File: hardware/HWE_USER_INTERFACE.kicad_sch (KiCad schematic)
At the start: 19 parts, among them J10 OLED_DISPLAY_i2c, J11 ENC_VOLUME_LED-RING, J13 OLED_DISPLAY_SPI, J4 BTN_PLAY, J5 BTN_REC, J6 BTN_STOP, J7 BTN_QUANTISE, J8 BTN_OVERDUB, J9 BTN_METRONOME

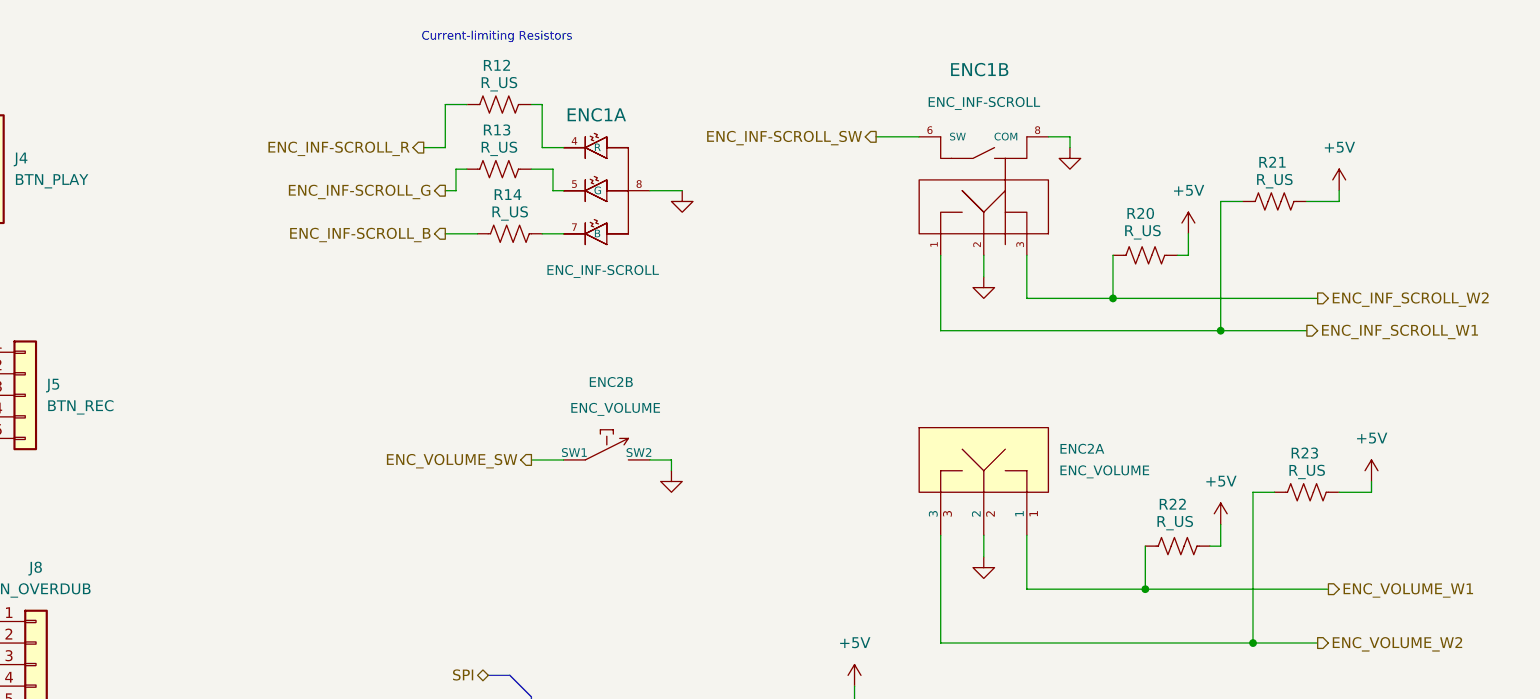
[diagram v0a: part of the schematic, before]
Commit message: fix [HWE]: Changed INF_SCROLL Enc to Enc + RGB LED
I have decided to switch from using this RGB LED encoder for the infinite scroll encoder to using a regular Rotary Encoder ( same as the Volume Encoder) with an associated common cathode RGB LED - it has the same functions, its just that this time it becomes so much easier to deal with in firmware. I was having massive troubles with the RGB encoder above as it was common anode for both switch and LEDs, and the Rotary Encoder itself used a different schema to that of my regular KY-040 rotary Encoders.

In fact I am even considering just using these KY-040 modules instead of routing out my own PEC11s to my PCB
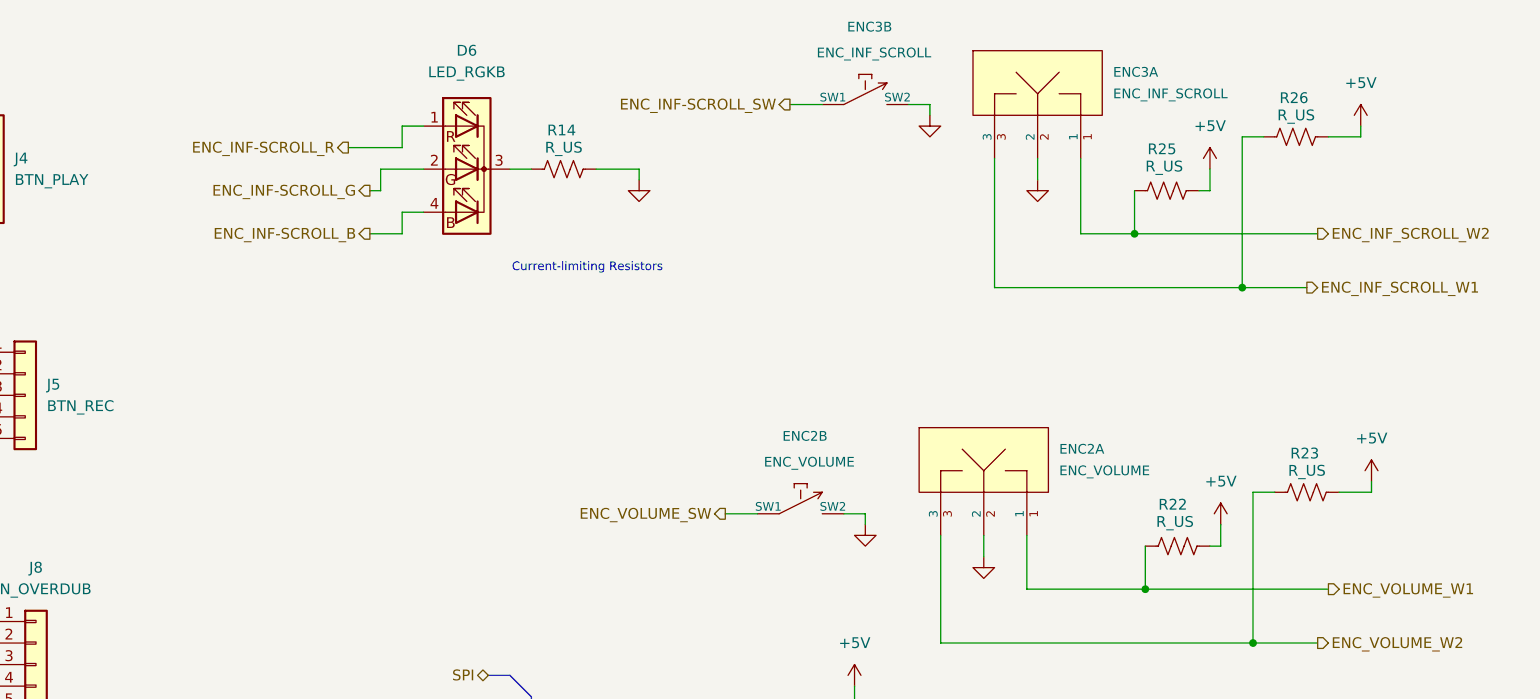
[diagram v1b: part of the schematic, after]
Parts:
- removed ENC1: ENC_INF-SCROLL, 4ms_Encoder:ENC_RGB_SPST_12mm, symbol 4ms_Switch:RGB_ROTARY_ENCODER-4ms-mech
- removed R12, R13, R20, R21: R_US, symbol Device:R_US
- added D6: LED_RGKB, LED_THT:LED_D5.0mm-4_RGB_Staggered_Pins, symbol Device:LED_RGKB
- added ENC3: ENC_INF_SCROLL, 4ms_Encoder:ENC_SPST_12mm, symbol 4ms_Switch:Encoder_Rotary_11mm_SPST_DShaft
- added R25, R26: R_US, symbol Device:R_US
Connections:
- net +5V: now also R25.2, R26.2
- net ENC_INF-SCROLL_B: now also D6.4 (BA); no longer R14.1
- net ENC_INF-SCROLL_G: now also D6.2 (GA)
- net ENC_INF-SCROLL_R: now also D6.1 (RA)
- net ENC_INF-SCROLL_SW: now also ENC3.SW1
- net ENC_INF_SCROLL_W1: now also ENC3.3, R26.1
- net ENC_INF_SCROLL_W2: now also ENC3.1, R25.1
- net GND: now also R14.2, ENC3.2, ENC3.SW2
- new net: D6.3 (K), R14.1
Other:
- moved on the sheet: ENC2B, R14

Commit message: misc [hwe]: Fixed INF_SCROLL ENC RGB LED
It was the incorrect configuration. The ones I have have the pin out of Pin 1 = Red, 2 = Common Cathode, 3 = Green, 4 = Blue
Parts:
- D6: value LED_RGKB -> LED_RKGB; symbol Device:LED_RGKB -> Device:LED_RKGB
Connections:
- net ENC_INF-SCROLL_G: now also D6.3 (GA); no longer D6.2 (GA)
- net at R14.1: now also D6.2 (K); no longer D6.3 (K)
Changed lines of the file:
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@@
 	)
 	(symbol
-		(lib_id "Device:LED_RGKB")
+		(lib_id "Device:LED_RKGB")
 		(at 162.56 31.75 0)
 		(mirror y)
@@
 			)
 		)
-		(property "Value" "LED_RGKB"
+		(property "Value" "LED_RKGB"
 			(at 162.56 20.32 0)
 			(effects
@@
 			)
 		)
-		(property "Description" "RGB LED, red/green/cathode/blue"
+		(property "Description" "RGB LED, red/cathode/green/blue"
 			(at 162.56 31.75 0)
 			(effects

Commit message: feat [HWE]: Attached LED_RING VCC to FET SWITCH
Attached the LED_RING VCC and VIO pins to a FET switch which is driven by the MCU's RESET pin as I was noticing during prototyping a bug that whenever I went into bootloader mode on the ESP32-S3, the system will not send any i2c LED turn off signals to the LED Ring
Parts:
- added Q3: 2N7002K, 4ms_Package_SOT:SOT-23, symbol 4ms_Transistor:2N7002K
- added R27, R28: R_US, symbol Device:R_US
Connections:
- net +5V: now also R28.1; no longer J11.1 (Pin_1), J11.3 (Pin_3)
- new net: Q3.3 (D), R27.2, R28.2
- new net +3.3V: R27.1
- new net LED_RING_FET: J11.1 (Pin_1), J11.3 (Pin_3), Q3.2 (S)
- new net LED_RING_VCC_RESET: Q3.1 (G)
